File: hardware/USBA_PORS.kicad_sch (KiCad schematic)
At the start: 21 parts, among them J1 0483930003, J2 0483930003, J3 0483930003, J4 0483930003

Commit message: finnished rudimentry schimatics still needs alot of work
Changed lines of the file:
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@@
   (symbol (lib_id "CARTHING:USB5916C") (at 45.72 50.8 0) (unit 6)
     (in_bom yes) (on_board yes) (dnp no)
-    (property "Reference" "U12" (at 46.0382 62.865 90)
+    (property "Reference" "U12" (at 48.26 63.5 0)
       (effects (font (size 1.27 1.27)) (justify right))
     )
@@
   (symbol (lib_id "CARTHING:0483930003") (at 256.54 121.92 0) (mirror x) (unit 1)
     (in_bom yes) (on_board yes) (dnp no)
-    (property "Reference" "J4" (at 267.97 102.219 0)
+    (property "Reference" "J4" (at 243.84 104.14 0)
       (effects (font (size 1.27 1.27)) (justify right))
     )
@@
   (symbol (lib_id "CARTHING:0483930003") (at 118.11 46.99 0) (mirror x) (unit 1)
     (in_bom yes) (on_board yes) (dnp no)
-    (property "Reference" "J1" (at 128.27 26.67 0)
+    (property "Reference" "J1" (at 105.41 29.21 0)
       (effects (font (size 1.27 1.27)) (justify right))
     )
@@
   (symbol (lib_id "CARTHING:0483930003") (at 118.11 127 0) (mirror x) (unit 1)
     (in_bom yes) (on_board yes) (dnp no)
-    (property "Reference" "J3" (at 128.27 107.299 0)
+    (property "Reference" "J3" (at 105.41 109.22 0)
       (effects (font (size 1.27 1.27)) (justify right))
     )
@@
   (symbol (lib_id "CARTHING:0483930003") (at 266.7 46.99 0) (mirror x) (unit 1)
     (in_bom yes) (on_board yes) (dnp no)
-    (property "Reference" "J2" (at 278.13 26.67 0)
-      (effects (font (size 1.27 1.27)) (justify right))
-    )
+    (property "Reference" "J2" (at 254 29.21 0)
+      (effects (font (size 1.27 1.27)) (justify right))
+    )

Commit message: working on hardware
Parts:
- added C97 (x4), C98 (x4): 0.1uF, Capacitor_SMD:C_0603_1608Metric, symbol Device:C
- D10: renamed from D6; footprint (none) -> Diode_SMD:D_0603_1608Metric
- D15: renamed from D8; footprint (none) -> Diode_SMD:D_0603_1608Metric
- D16: renamed from D9; footprint (none) -> Diode_SMD:D_0603_1608Metric
- D9: renamed from D7; footprint (none) -> Diode_SMD:D_0603_1608Metric
- F1: footprint (none) -> Fuse:Fuse_1812_4532Metric
- F2: renamed from F4; footprint (none) -> Fuse:Fuse_1812_4532Metric
- F3: renamed from F2; footprint (none) -> Fuse:Fuse_1812_4532Metric
- F4: renamed from F3; footprint (none) -> Fuse:Fuse_1812_4532Metric
- renumbered D14 to D11, D17 to D12, D11 to D14, D15 to D17, D16 to D18, D10 to D8, D12 to De1, J1 to J3, J3 to J4, J2 to J5, J4 to J6, U12 to U13
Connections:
- net P2_RX_N: now also C98.2; no longer J3.5 (STDA_SSRX-)
- net P2_RX_P: now also C97.1; no longer J3.6 (STDA_SSRX+)
- net P3_RX_N: now also C98.2; no longer J5.5 (STDA_SSRX-)
- net P3_RX_P: now also C97.1; no longer J5.6 (STDA_SSRX+)
- net P4_RX_N: now also C98.2; no longer J4.5 (STDA_SSRX-)
- net P4_RX_P: now also C97.1; no longer J4.6 (STDA_SSRX+)
- net P5_RX_N: now also C98.2; no longer J6.5 (STDA_SSRX-)
- net P5_RX_P: now also C97.1; no longer J6.6 (STDA_SSRX+)
- new net: C98.1, J4.5 (STDA_SSRX-)
- new net: C97.2, J5.6 (STDA_SSRX+)
- new net: C98.1, J6.5 (STDA_SSRX-)
- new net: C97.2, J6.6 (STDA_SSRX+)
- new net: C98.1, J3.5 (STDA_SSRX-)
- new net: C97.2, J3.6 (STDA_SSRX+)
- new net: C97.2, J4.6 (STDA_SSRX+)
- new net: C98.1, J5.5 (STDA_SSRX-)
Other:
- moved on the sheet: D13, D14, D15, D16, D17, D18, D8, De1, F3, F4, J5, J6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

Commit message: FINALY starting the pcb
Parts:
- D11, D12, D17, D18: footprint Diode_SMD_AKL:D_SOD-523 -> Diode_SMD:D_0603_1608Metric
- D13, D14, D8: footprint (none) -> CARTHING:PUSB3AB6Z_NEX
- D35: renamed from De1; footprint (none) -> CARTHING:PUSB3AB6Z_NEX
- J3, J4, J5, J6: footprint 0483930003:MOLEX_0483930003 -> CARTHING:MOLEX_0483930003
- U13: footprint (none) -> CARTHING:VQFN100_KD_MCH
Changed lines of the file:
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@@
       (effects (font (size 1.27 1.27)))
     )
-    (property "Footprint" "" (at 195.58 107.95 0)
+    (property "Footprint" "CARTHING:PUSB3AB6Z_NEX" (at 195.58 107.95 0)
       (effects (font (size 1.27 1.27)) hide)
     )
@@
       (effects (font (size 1.27 1.27)))
     )
-    (property "Footprint" "" (at 170.18 19.05 0)
+    (property "Footprint" "CARTHING:VQFN100_KD_MCH" (at 170.18 19.05 0)
       (effects (font (size 1.27 1.27)) hide)
     )
@@
       (effects (font (size 1.27 1.27)))
     )
-    (property "Footprint" "" (at 33.02 19.05 0)
+    (property "Footprint" "CARTHING:VQFN100_KD_MCH" (at 33.02 19.05 0)
       (effects (font (size 1.27 1.27)) hide)
     )
@@
       (effects (font (size 1.27 1.27)) (justify right))
     )
-    (property "Footprint" "0483930003:MOLEX_0483930003" (at 261.62 140.97 0)
+    (property "Footprint" "CARTHING:MOLEX_0483930003" (at 261.62 140.97 0)
       (effects (font (size 1.27 1.27)) (justify bottom) hide)
     )
@@
       (effects (font (size 1.27 1.27)))
     )
-    (property "Footprint" "" (at 59.69 33.02 0)
+    (property "Footprint" "CARTHING:PUSB3AB6Z_NEX" (at 59.69 33.02 0)
       (effects (font (size 1.27 1.27)) hide)
     )
@@
       (effects (font (size 1.27 1.27)) (justify right))
     )
-    (property "Footprint" "0483930003:MOLEX_0483930003" (at 118.11 66.04 0)
+    (property "Footprint" "CARTHING:MOLEX_0483930003" (at 118.11 66.04 0)
       (effects (font (size 1.27 1.27)) (justify bottom) hide)
     )
@@
       (effects (font (size 1.27 1.27)) (justify right))
     )
-    (property "Footprint" "0483930003:MOLEX_0483930003" (at 118.11 146.05 0)
+    (property "Footprint" "CARTHING:MOLEX_0483930003" (at 118.11 146.05 0)
       (effects (font (size 1.27 1.27)) (justify bottom) hide)
     )
@@
   (symbol (lib_id "CARTHING:PUSB3FR6") (at 76.2 106.68 90) (unit 1)
     (in_bom yes) (on_board yes) (dnp no) (fields_autoplaced)
-    (property "Reference" "De1" (at 76.835 100.6381 90)
+    (property "Reference" "D35" (at 76.835 100.6381 90)
       (effects (font (size 1.27 1.27)))
     )
@@
       (effects (font (size 1.27 1.27)))
     )
-    (property "Footprint" "" (at 58.42 113.03 0)
+    (property "Footprint" "CARTHING:PUSB3AB6Z_NEX" (at 58.42 113.03 0)
       (effects (font (size 1.27 1.27)) hide)
     )
@@
       (project "usbc-car-module"
         (path "/fae025e9-99c5-40c1-af6f-99dc1edbfa43/fe8e7353-13b3-4aa6-97f7-d88e32d23b04"
-          (reference "De1") (unit 1)
+          (reference "D35") (unit 1)
         )
       )
@@
       (effects (font (size 1.27 1.27)) (justify right))
     )
-    (property "Footprint" "Diode_SMD_AKL:D_SOD-523" (at 269.24 151.13 0)
+    (property "Footprint" "Diode_SMD:D_0603_1608Metric" (at 269.24 151.13 0)
       (effects (font (size 1.27 1.27)) hide)
     )
@@
       (effects (font (size 1.27 1.27)))
     )
-    (property "Footprint" "" (at 168.91 93.98 0)
+    (property "Footprint" "CARTHING:VQFN100_KD_MCH" (at 168.91 93.98 0)
       (effects (font (size 1.27 1.27)) hide)
     )
@@
       (effects (font (size 1.27 1.27)))
     )
-    (property "Footprint" "" (at 31.75 99.06 0)
+    (property "Footprint" "CARTHING:VQFN100_KD_MCH" (at 31.75 99.06 0)
       (effects (font (size 1.27 1.27)) hide)
     )
@@
       (effects (font (size 1.27 1.27)) (justify right))
     )
-    (property "Footprint" "Diode_SMD_AKL:D_SOD-523" (at 125.73 76.2 0)
+    (property "Footprint" "Diode_SMD:D_0603_1608Metric" (at 125.73 76.2 0)
       (effects (font (size 1.27 1.27)) hide)
     )
@@
       (effects (font (size 1.27 1.27)) (justify right))
     )
-    (property "Footprint" "Diode_SMD_AKL:D_SOD-523" (at 269.24 76.2 0)
+    (property "Footprint" "Diode_SMD:D_0603_1608Metric" (at 269.24 76.2 0)
       (effects (font (size 1.27 1.27)) hide)
     )
@@
       (effects (font (size 1.27 1.27)) (justify right))
     )
-    (property "Footprint" "0483930003:MOLEX_0483930003" (at 261.62 66.04 0)
+    (property "Footprint" "CARTHING:MOLEX_0483930003" (at 261.62 66.04 0)
       (effects (font (size 1.27 1.27)) (justify bottom) hide)
     )
@@
       (effects (font (size 1.27 1.27)))
     )
-    (property "Footprint" "" (at 200.66 33.02 0)
+    (property "Footprint" "CARTHING:PUSB3AB6Z_NEX" (at 200.66 33.02 0)
       (effects (font (size 1.27 1.27)) hide)
     )
@@
       (effects (font (size 1.27 1.27)) (justify right))
     )
-    (property "Footprint" "Diode_SMD_AKL:D_SOD-523" (at 125.73 156.21 0)
-      (effects (font (size 1.27 1.27)) hide)
-    )
+    (property "Footprint" "Diode_SMD:D_0603_1608Metric" (at 125.73 156.21 0)
+      (effects (font (size 1.27 1.27)) hide)
+    )

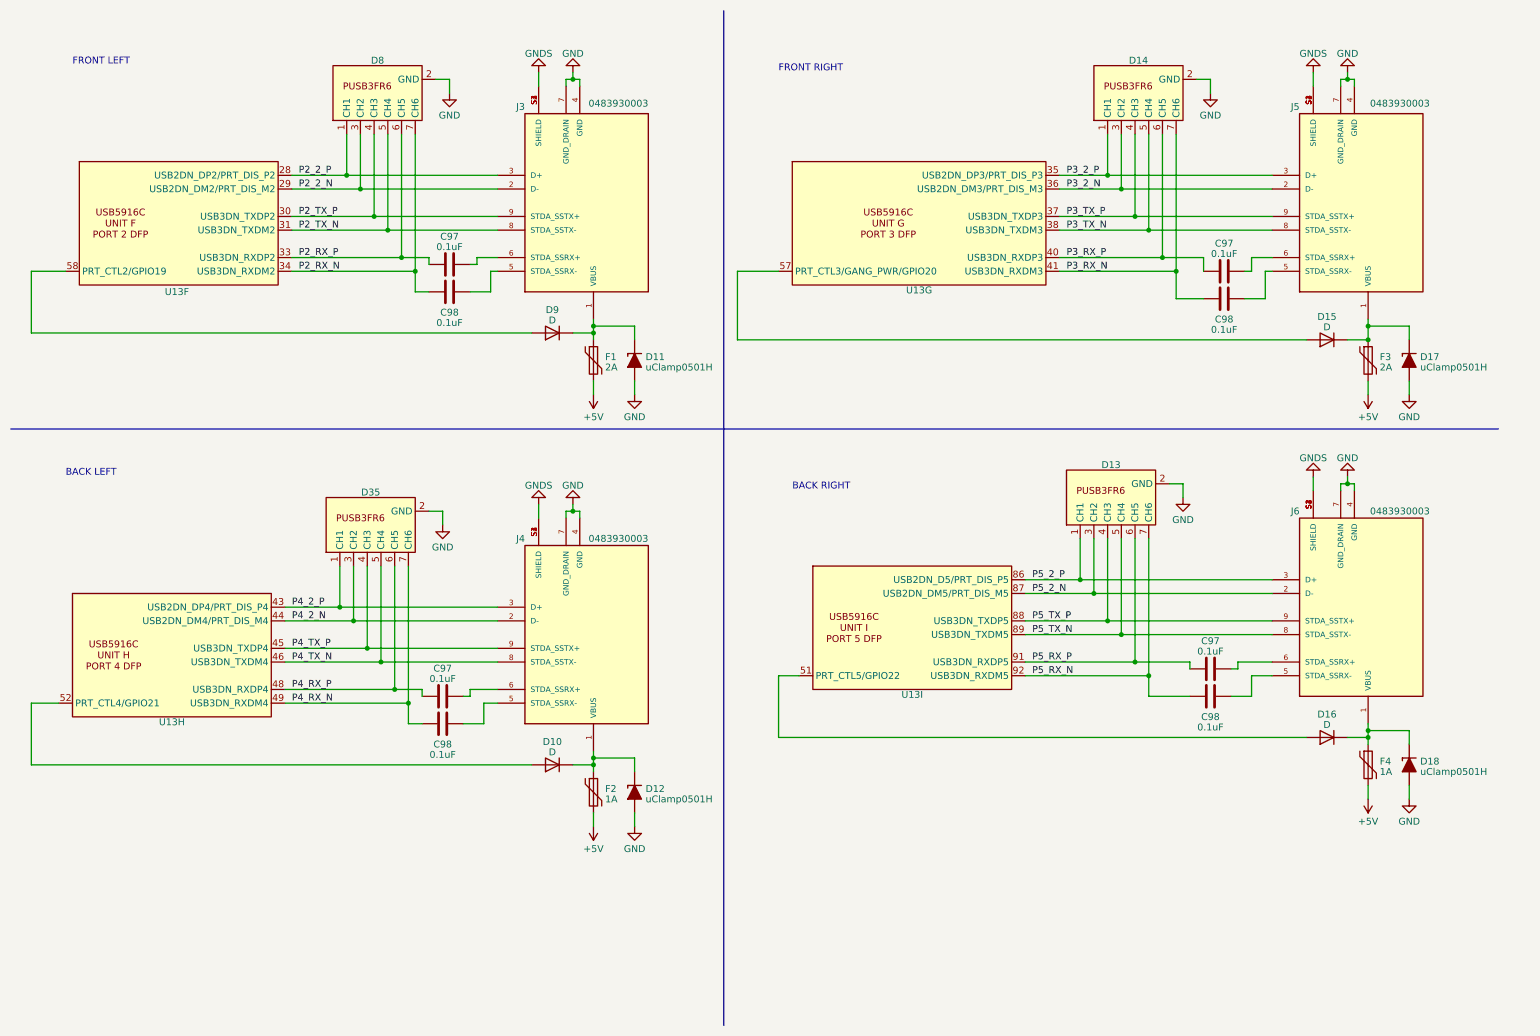
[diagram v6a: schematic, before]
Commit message: worked on usb port and display routing
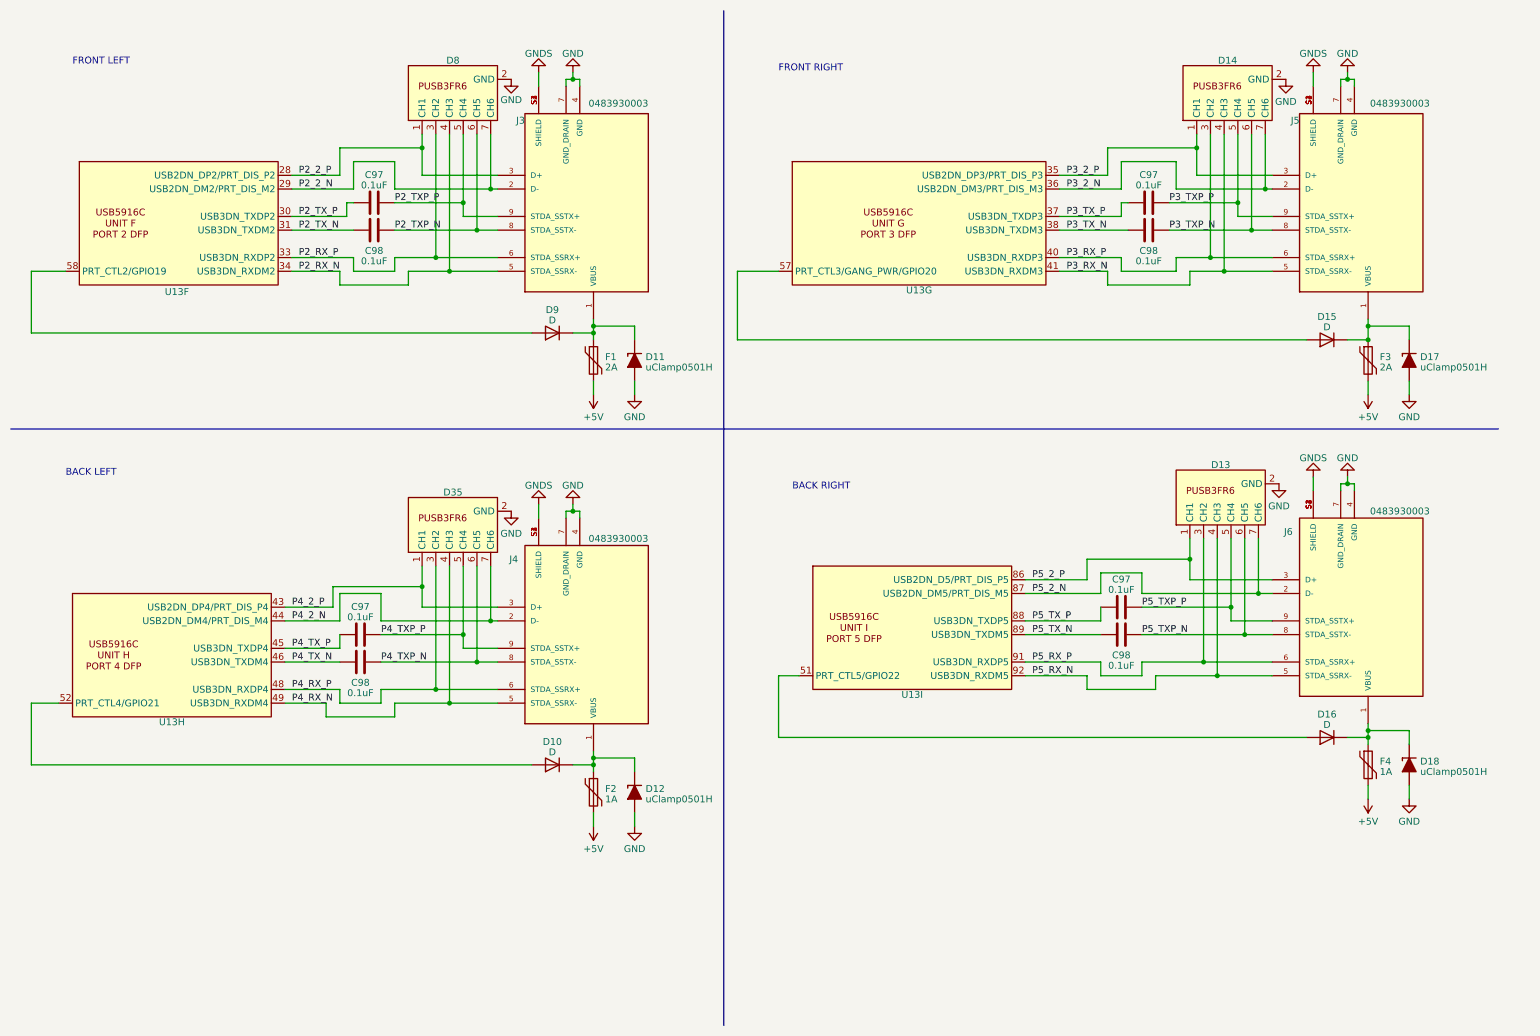
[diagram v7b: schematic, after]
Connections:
- net P2_2_N: now also D8.7 (CH6); no longer D8.3 (CH2)
- net P2_RX_N: now also D8.4 (CH3), J3.5 (STDA_SSRX-); no longer C98.2, D8.7 (CH6)
- net P2_RX_P: now also D8.3 (CH2), J3.6 (STDA_SSRX+); no longer C97.1, D8.6 (CH5)
- net P2_TX_N: now also C98.2; no longer D8.5 (CH4), J3.8 (STDA_SSTX-)
- net P2_TX_P: now also C97.1; no longer D8.4 (CH3), J3.9 (STDA_SSTX+)
- net P3_2_N: now also D14.7 (CH6); no longer D14.3 (CH2)
- net P3_RX_N: now also D14.4 (CH3), J5.5 (STDA_SSRX-); no longer C98.2, D14.7 (CH6)
- net P3_RX_P: now also D14.3 (CH2), J5.6 (STDA_SSRX+); no longer C97.1, D14.6 (CH5)
- net P3_TX_N: now also C98.2; no longer D14.5 (CH4), J5.8 (STDA_SSTX-)
- net P3_TX_P: now also C97.1; no longer D14.4 (CH3), J5.9 (STDA_SSTX+)
- net P4_2_N: now also D35.7 (CH6); no longer D35.3 (CH2)
- net P4_RX_N: now also D35.4 (CH3), J4.5 (STDA_SSRX-); no longer C98.2, D35.7 (CH6)
- net P4_RX_P: now also D35.3 (CH2), J4.6 (STDA_SSRX+); no longer C97.1, D35.6 (CH5)
- net P4_TX_N: now also C98.2; no longer D35.5 (CH4), J4.8 (STDA_SSTX-)
- net P4_TX_P: now also C97.1; no longer D35.4 (CH3), J4.9 (STDA_SSTX+)
- net P5_2_N: now also D13.7 (CH6); no longer D13.3 (CH2)
- net P5_RX_N: now also D13.4 (CH3), J6.5 (STDA_SSRX-); no longer C98.2, D13.7 (CH6)
- net P5_RX_P: now also D13.3 (CH2), J6.6 (STDA_SSRX+); no longer C97.1, D13.6 (CH5)
- net P5_TX_N: now also C98.2; no longer D13.5 (CH4), J6.8 (STDA_SSTX-)
- net P5_TX_P: now also C97.1; no longer D13.4 (CH3), J6.9 (STDA_SSTX+)
- net P4_TXP_N: now reaches C98.1
- net P4_TXP_N: now also D35.6 (CH5), J4.8 (STDA_SSTX-); no longer J4.5 (STDA_SSRX-)
- net P3_TXP_P: now reaches C97.2
- net P3_TXP_P: now also D14.5 (CH4), J5.9 (STDA_SSTX+); no longer J5.6 (STDA_SSRX+)
- net P5_TXP_N: now reaches C98.1
- net P5_TXP_N: now also D13.6 (CH5), J6.8 (STDA_SSTX-); no longer J6.5 (STDA_SSRX-)
- net P5_TXP_P: now reaches C97.2
- net P5_TXP_P: now also D13.5 (CH4), J6.9 (STDA_SSTX+); no longer J6.6 (STDA_SSRX+)
- net P2_TXP_N: now reaches C98.1
- net P2_TXP_N: now also D8.6 (CH5), J3.8 (STDA_SSTX-); no longer J3.5 (STDA_SSRX-)
- net P2_TXP_P: now reaches C97.2
- net P2_TXP_P: now also D8.5 (CH4), J3.9 (STDA_SSTX+); no longer J3.6 (STDA_SSRX+)
- net P4_TXP_P: now reaches C97.2
- net P4_TXP_P: now also D35.5 (CH4), J4.9 (STDA_SSTX+); no longer J4.6 (STDA_SSRX+)
- net P3_TXP_N: now reaches C98.1
- net P3_TXP_N: now also D14.6 (CH5), J5.8 (STDA_SSTX-); no longer J5.5 (STDA_SSRX-)
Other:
- moved on the sheet: C97, C98, D13, D14, D35, D8

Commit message: working in final routing
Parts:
- J3, J4, J5, J6: footprint CARTHING:MOLEX_0483930003 -> 0483930003:MOLEX_0483930003
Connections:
- net GNDS: now also J3.S (SHIELD), J4.S (SHIELD), J5.S (SHIELD), J6.S (SHIELD); no longer J3.S1 (SHIELD), J3.S2 (SHIELD), J3.S3 (SHIELD), J3.S4 (SHIELD), J4.S1 (SHIELD), J4.S2 (SHIELD), J4.S3 (SHIELD), J4.S4 (SHIELD), J5.S1 (SHIELD), J5.S2 (SHIELD), J5.S3 (SHIELD), J5.S4 (SHIELD), J6.S1 (SHIELD), J6.S2 (SHIELD), J6.S3 (SHIELD), J6.S4 (SHIELD)
- net P2_2_N: now also U13.36 (USB2DN_DM3/PRT_DIS_M3); no longer U13.29 (USB2DN_DM2/PRT_DIS_M2)
- net P2_2_P: now also U13.35 (USB2DN_DP3/PRT_DIS_P3); no longer U13.28 (USB2DN_DP2/PRT_DIS_P2)
- net P2_RX_N: now also U13.41 (USB3DN_RXDM3); no longer U13.34 (USB3DN_RXDM2)
- net P2_RX_P: now also U13.40 (USB3DN_RXDP3); no longer U13.33 (USB3DN_RXDP2)
- net P2_TX_N: now also U13.38 (USB3DN_TXDM3); no longer U13.31 (USB3DN_TXDM2)
- net P2_TX_P: now also U13.37 (USB3DN_TXDP3); no longer U13.30 (USB3DN_TXDP2)
- net P3_2_N: now also U13.44 (USB2DN_DM4/PRT_DIS_M4); no longer U13.36 (USB2DN_DM3/PRT_DIS_M3)
- net P3_2_P: now also U13.43 (USB2DN_DP4/PRT_DIS_P4); no longer U13.35 (USB2DN_DP3/PRT_DIS_P3)
- net P3_RX_N: now also U13.49 (USB3DN_RXDM4); no longer U13.41 (USB3DN_RXDM3)
- net P3_RX_P: now also U13.48 (USB3DN_RXDP4); no longer U13.40 (USB3DN_RXDP3)
- net P3_TX_N: now also U13.46 (USB3DN_TXDM4); no longer U13.38 (USB3DN_TXDM3)
- net P3_TX_P: now also U13.45 (USB3DN_TXDP4); no longer U13.37 (USB3DN_TXDP3)
- net P4_2_N: now also U13.87 (USB2DN_DM5/PRT_DIS_M5); no longer U13.44 (USB2DN_DM4/PRT_DIS_M4)
- net P4_2_P: now also U13.86 (USB2DN_D5/PRT_DIS_P5); no longer U13.43 (USB2DN_DP4/PRT_DIS_P4)
- net P4_RX_N: now also U13.92 (USB3DN_RXDM5); no longer U13.49 (USB3DN_RXDM4)
- net P4_RX_P: now also U13.91 (USB3DN_RXDP5); no longer U13.48 (USB3DN_RXDP4)
- net P4_TX_N: now also U13.89 (USB3DN_TXDM5); no longer U13.46 (USB3DN_TXDM4)
- net P4_TX_P: now also U13.88 (USB3DN_TXDP5); no longer U13.45 (USB3DN_TXDP4)
- net P5_2_N: now also U13.29 (USB2DN_DM2/PRT_DIS_M2); no longer U13.87 (USB2DN_DM5/PRT_DIS_M5)
- net P5_2_P: now also U13.28 (USB2DN_DP2/PRT_DIS_P2); no longer U13.86 (USB2DN_D5/PRT_DIS_P5)
- net P5_RX_N: now also U13.34 (USB3DN_RXDM2); no longer U13.92 (USB3DN_RXDM5)
- net P5_RX_P: now also U13.33 (USB3DN_RXDP2); no longer U13.91 (USB3DN_RXDP5)
- net P5_TX_N: now also U13.31 (USB3DN_TXDM2); no longer U13.89 (USB3DN_TXDM5)
- net P5_TX_P: now also U13.30 (USB3DN_TXDP2); no longer U13.88 (USB3DN_TXDP5)
- net at U13.57 (PRT_CTL3/GANG_PWR/GPIO20): now also D9.2 (A); no longer D15.2 (A)
- net at U13.58 (PRT_CTL2/GPIO19): now also D16.2 (A); no longer D9.2 (A)
- net at U13.51 (PRT_CTL5/GPIO22): now also D10.2 (A); no longer D16.2 (A)
- net at U13.52 (PRT_CTL4/GPIO21): now also D15.2 (A); no longer D10.2 (A)
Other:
- moved on the sheet: C97, C98, D11, D8, D9, F1, U13F, U13G, U13H, U13I
